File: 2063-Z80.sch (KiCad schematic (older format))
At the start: 80 parts, among them J1 Conn_01x05, J10 Conn_01x07, J11 Conn_02x03, J2 DM3D-SF(41), J3 Conn_02x20, J4 Conn_02x05, J5 Conn_02x05, J6 0548190519, J7 Conn_02x13, J8 Conn_01x05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

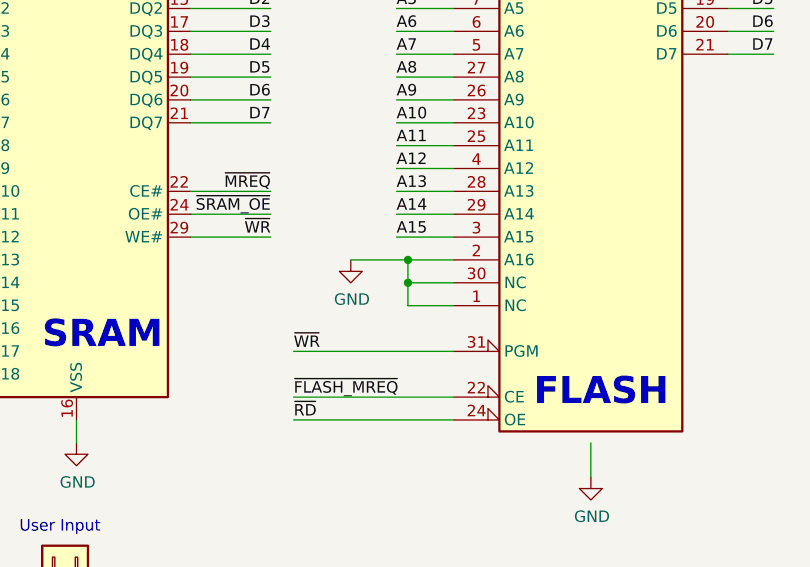
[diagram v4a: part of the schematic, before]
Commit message: Make pins U3.1 & U3.30 NC (easier for UV EPROM)
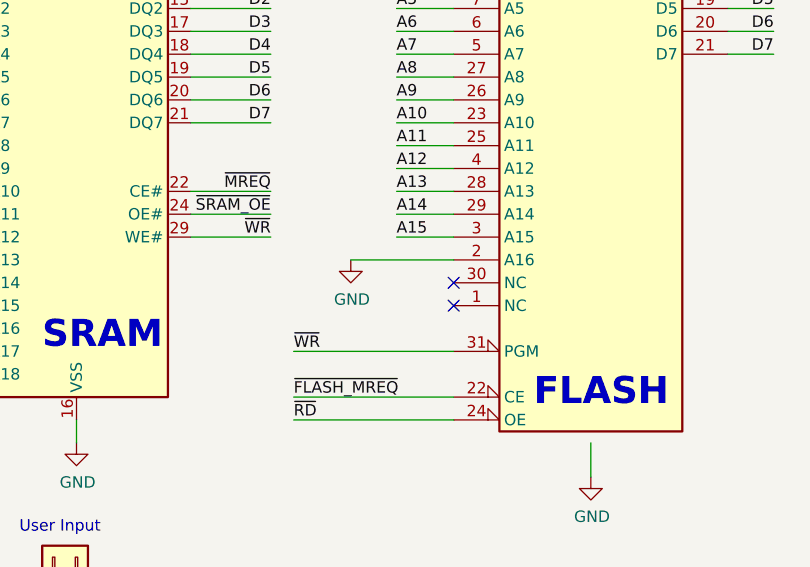
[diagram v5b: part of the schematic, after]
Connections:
- net GND: no longer U3.1 (NC), U3.30 (NC)
- no-connect marks 32 -> 34
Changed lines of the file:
@@
 Wire Wire Line
 	11050 9650 11050 9500
-Wire Wire Line
-	5400 4000 5200 4000
-Wire Wire Line
-	5200 4000 5200 4100
-Wire Wire Line
-	5400 4100 5200 4100
-Connection ~ 5200 4100
-Wire Wire Line
-	5200 4100 5200 4200
-Wire Wire Line
-	5400 4200 5200 4200
 $Comp
 L power:+5V #PWR0141
@@
 	1    0    0    -1
 $EndComp
-Wire Wire Line
-	6000 4800 6000 4950
 Text Label 4700 4600 0    50   ~ 0
 ~FLASH_MREQ
@@
 	1    0    0    -1
 $EndComp
-Wire Wire Line
-	4950 4000 5200 4000
-Connection ~ 5200 4000
 Wire Wire Line
 	8100 6100 8450 6100
@@
 $EndComp
 $Comp
-L Memory_Flash:SST39SF010 U3
-U 1 1 62897764
-P 6000 3600
-F 0 "U3" H 6450 5050 50  0000 C CNN
-F 1 "SST39SF010" H 6450 4950 50  0000 C CNN
-F 2 "Package_DIP:DIP-32_W15.24mm_Socket" H 6000 3900 50  0001 C CNN
-F 3 "https://ww1.microchip.com/downloads/en/DeviceDoc/20005022C.pdf" H 6000 3900 50  0001 C CNN
-F 4 "IC FLASH 1MBIT PARALLEL 32DIP" H 6000 3600 50  0001 C CNN "Description"
-F 5 "SST39SF010A-70-4C-PHE-ND‎" H 6000 3600 50  0001 C CNN "Digi-Key_PN"
-F 6 "SST39SF010A-70-4C-PHE" H 6000 3600 50  0001 C CNN "MPN"
-F 7 "Microchip Technology" H 6000 3600 50  0001 C CNN "Manufacturer"
-	1    6000 3600
-	1    0    0    -1
-$EndComp
-$Comp
 L Device:R_Network08 RN2
 U 1 1 61079B79
@@
 Text Label 13850 6550 2    50   ~ 0
 ~DTRB
+Wire Wire Line
+	4950 4000 5400 4000
+Wire Wire Line
+	6000 4800 6000 4950
+$Comp
+L Memory_Flash:SST39SF010 U3
+U 1 1 62897764
+P 6000 3600
+F 0 "U3" H 6450 5050 50  0000 C CNN
+F 1 "SST39SF010" H 6450 4950 50  0000 C CNN
+F 2 "Package_DIP:DIP-32_W15.24mm_Socket" H 6000 3900 50  0001 C CNN
+F 3 "https://ww1.microchip.com/downloads/en/DeviceDoc/20005022C.pdf" H 6000 3900 50  0001 C CNN
+F 4 "IC FLASH 1MBIT PARALLEL 32DIP" H 6000 3600 50  0001 C CNN "Description"
+F 5 "SST39SF010A-70-4C-PHE-ND‎" H 6000 3600 50  0001 C CNN "Digi-Key_PN"
+F 6 "SST39SF010A-70-4C-PHE" H 6000 3600 50  0001 C CNN "MPN"
+F 7 "Microchip Technology" H 6000 3600 50  0001 C CNN "Manufacturer"
+	1    6000 3600
+	1    0    0    -1
+$EndComp
+NoConn ~ 5400 4100
+NoConn ~ 5400 4200
 $EndSCHEMATC

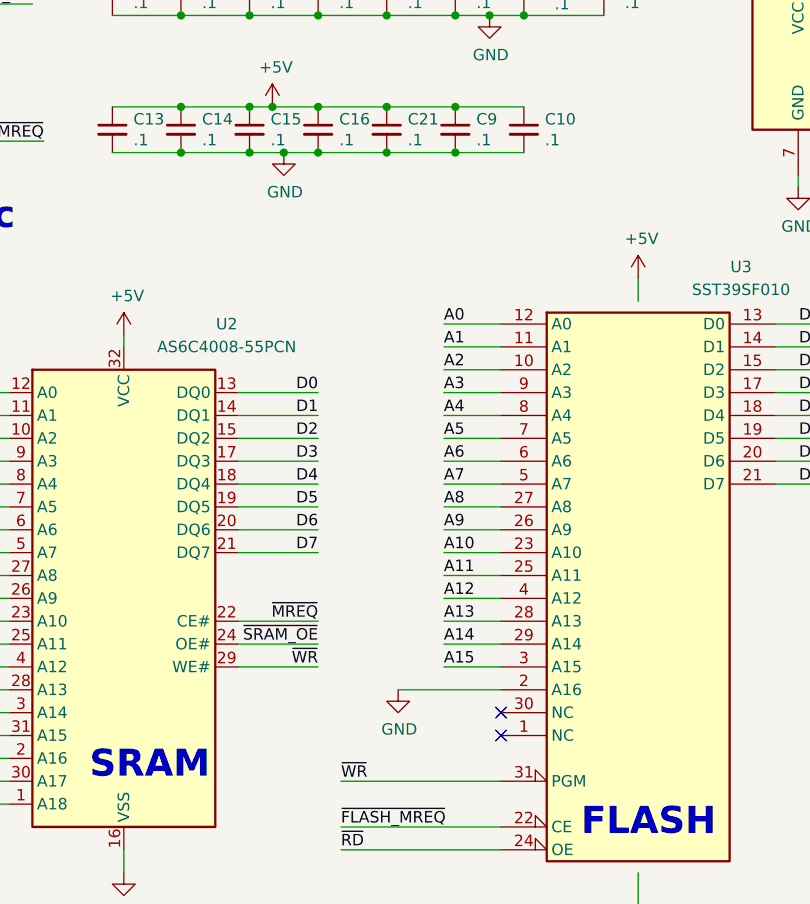
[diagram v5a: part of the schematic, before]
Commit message: Add pulldown & J12 to A16 for FLASH bank select
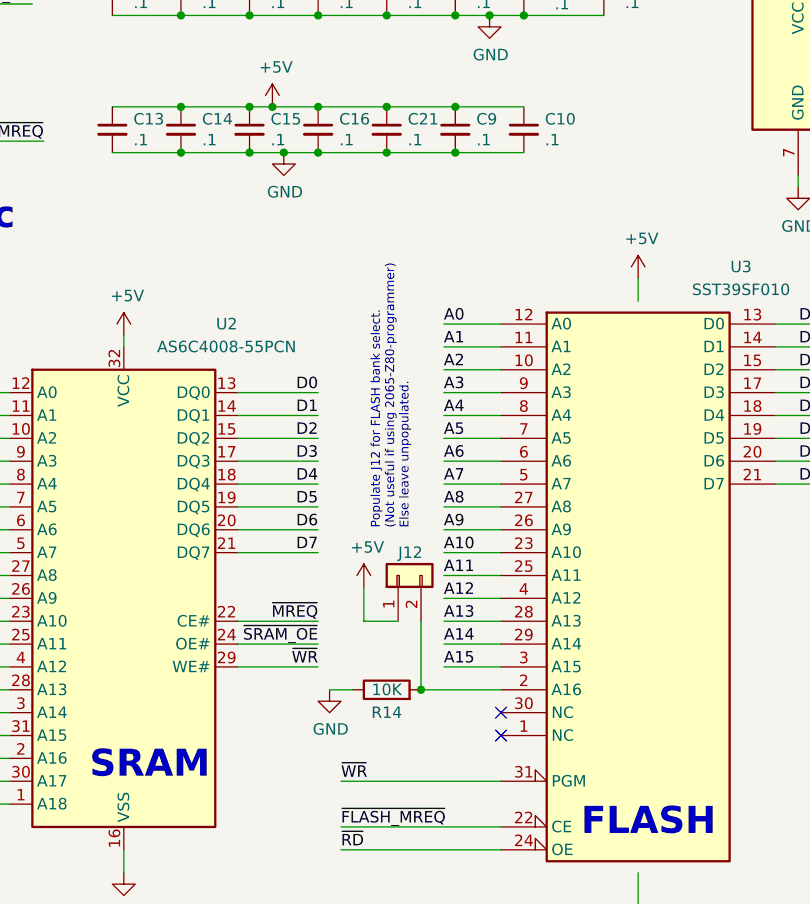
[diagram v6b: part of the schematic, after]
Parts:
- added J12: Conn_01x02, Connector_PinHeader_2.54mm:PinHeader_1x02_P2.54mm_Vertical, symbol Connector_Generic:Conn_01x02
- added R14: 10K, Resistor_THT:R_Axial_DIN0204_L3.6mm_D1.6mm_P5.08mm_Horizontal, symbol Device:R
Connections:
- net +5V: now also J12.1 (Pin_1)
- net GND: now also R14.1; no longer U3.2 (A16)
- new net: J12.2 (Pin_2), R14.2, U3.2 (A16)
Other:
- note added: "Populate J12 for FLASH bank select.\n(Not useful if using 2065-Z80-programmer)\nElse leave unpopulated."
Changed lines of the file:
@@
 L power:GND #PWR010
 U 1 1 62F49F76
-P 4950 4000
-F 0 "#PWR010" H 4950 3750 50  0001 C CNN
-F 1 "GND" H 4955 3827 50  0000 C CNN
-F 2 "" H 4950 4000 50  0001 C CNN
-F 3 "" H 4950 4000 50  0001 C CNN
-	1    4950 4000
+P 4650 4000
+F 0 "#PWR010" H 4650 3750 50  0001 C CNN
+F 1 "GND" H 4655 3827 50  0000 C CNN
+F 2 "" H 4650 4000 50  0001 C CNN
+F 3 "" H 4650 4000 50  0001 C CNN
+	1    4650 4000
 	1    0    0    -1
 $EndComp
@@
 ~DTRB
 Wire Wire Line
-	4950 4000 5400 4000
-Wire Wire Line
 	6000 4800 6000 4950
 $Comp
@@
 NoConn ~ 5400 4100
 NoConn ~ 5400 4200
+$Comp
+L Device:R R14
+U 1 1 61ED6941
+P 4900 4000
+F 0 "R14" V 4800 4000 50  0000 C CNN
+F 1 "10K" V 4900 4000 50  0000 C CNN
+F 2 "Resistor_THT:R_Axial_DIN0204_L3.6mm_D1.6mm_P5.08mm_Horizontal" V 4830 4000 50  0001 C CNN
+F 3 "https://www.seielect.com/catalog/sei-cf_cfm.pdf" H 4900 4000 50  0001 C CNN
+F 4 "RES 10K OHM 5% 1/8W AXIAL" H 4900 4000 50  0001 C CNN "Description"
+F 5 "CF18JT10K0CT-ND" H 4900 4000 50  0001 C CNN "Digi-Key_PN"
+F 6 "CF18JT10K0" H 4900 4000 50  0001 C CNN "MPN"
+F 7 "Stackpole Electronics Inc" H 4900 4000 50  0001 C CNN "Manufacturer"
+	1    4900 4000
+	0    -1   -1   0
+$EndComp
+Wire Wire Line
+	4650 4000 4750 4000
+$Comp
+L Connector_Generic:Conn_01x02 J12
+U 1 1 62007C5F
+P 4950 3500
+F 0 "J12" V 5050 3500 50  0000 R CNN
+F 1 "Conn_01x02" V 4823 3312 50  0001 R CNN
+F 2 "Connector_PinHeader_2.54mm:PinHeader_1x02_P2.54mm_Vertical" H 4950 3500 50  0001 C CNN
+F 3 "https://media.digikey.com/PDF/Data%20Sheets/Sullins%20PDFs/xRxCzzzSxxN-RC_ST_11635-B.pdf" H 4950 3500 50  0001 C CNN
+F 4 "CONN HEADER VERT 2POS 2.54MM" H 4950 3500 50  0001 C CNN "Description"
+F 5 "S1011EC-02-ND" H 4950 3500 50  0001 C CNN "Digi-Key_PN"
+F 6 "PRPC002SAAN-RC" H 4950 3500 50  0001 C CNN "MPN"
+F 7 "Sullins Connector Solutions" H 4950 3500 50  0001 C CNN "Manufacturer"
+	1    4950 3500
+	0    -1   -1   0
+$EndComp
+Wire Wire Line
+	5050 4000 5400 4000
+Connection ~ 5050 4000
+Wire Wire Line
+	4950 3700 4800 3700
+Wire Wire Line
+	4800 3700 4800 3550
+$Comp
+L power:+5V #PWR019
+U 1 1 62228824
+P 4800 3550
+F 0 "#PWR019" H 4800 3400 50  0001 C CNN
+F 1 "+5V" H 4815 3723 50  0000 C CNN
+F 2 "" H 4800 3550 50  0001 C CNN
+F 3 "" H 4800 3550 50  0001 C CNN
+	1    4800 3550
+	1    0    0    -1
+$EndComp
+Wire Wire Line
+	5050 3700 5050 4000
+Text Notes 5000 3300 1    39   ~ 0
+Populate J12 for FLASH bank select.\n(Not useful if using 2065-Z80-programmer)\nElse leave unpopulated.
 $EndSCHEMATC

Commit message: Terminate the clock traces.
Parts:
- added R15, R16: 120, Resistor_THT:R_Axial_DIN0204_L3.6mm_D1.6mm_P5.08mm_Horizontal, symbol Device:R
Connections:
- net BAUD_CLK: now also R16.2
- net CLK: now also R15.2
- net GND: now also R15.1, R16.1
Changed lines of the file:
@@
 CLK
 Wire Wire Line
-	9050 1200 9350 1200
+	9050 1200 9150 1200
 Text Label 9350 1200 2    50   ~ 0
 CLK
@@
 Connection ~ 12200 2200
 Wire Wire Line
-	12200 2200 12600 2200
-Wire Wire Line
 	11250 2900 12200 2900
 Wire Wire Line
@@
 Text Notes 5000 3300 1    39   ~ 0
 Populate J12 for FLASH bank select.\n(Not useful if using 2065-Z80-programmer)\nElse leave unpopulated.
+Wire Wire Line
+	9150 1500 9150 1200
+Connection ~ 9150 1200
+Wire Wire Line
+	9150 1200 9350 1200
+Wire Wire Line
+	9450 1500 9550 1500
+$Comp
+L power:GND #PWR020
+U 1 1 61C29EFA
+P 9550 1500
+F 0 "#PWR020" H 9550 1250 50  0001 C CNN
+F 1 "GND" H 9555 1327 50  0000 C CNN
+F 2 "" H 9550 1500 50  0001 C CNN
+F 3 "" H 9550 1500 50  0001 C CNN
+	1    9550 1500
+	1    0    0    -1
+$EndComp
+$Comp
+L Device:R R16
+U 1 1 61C3AA3E
+P 12850 2200
+F 0 "R16" V 12750 2200 50  0000 C CNN
+F 1 "120" V 12850 2200 50  0000 C CNN
+F 2 "Resistor_THT:R_Axial_DIN0204_L3.6mm_D1.6mm_P5.08mm_Horizontal" V 12780 2200 50  0001 C CNN
+F 3 "https://www.seielect.com/catalog/sei-cf_cfm.pdf" H 12850 2200 50  0001 C CNN
+F 4 "RES 120 OHM 5% 1/8W AXIAL" H 12850 2200 50  0001 C CNN "Description"
+F 5 "CF18JT120RCT-ND" H 12850 2200 50  0001 C CNN "Digi-Key_PN"
+F 6 "CF18JT120R" H 12850 2200 50  0001 C CNN "MPN"
+F 7 "Stackpole Electronics Inc" H 12850 2200 50  0001 C CNN "Manufacturer"
+	1    12850 2200
+	0    1    1    0
+$EndComp
+Wire Wire Line
+	13000 2200 13100 2200
+$Comp
+L power:GND #PWR021
+U 1 1 61C3AA46
+P 13100 2200
+F 0 "#PWR021" H 13100 1950 50  0001 C CNN
+F 1 "GND" H 13105 2027 50  0000 C CNN
+F 2 "" H 13100 2200 50  0001 C CNN
+F 3 "" H 13100 2200 50  0001 C CNN
+	1    13100 2200
+	1    0    0    -1
+$EndComp
+Wire Wire Line
+	12200 2200 12700 2200
+$Comp
+L Device:R R15
+U 1 1 61D53855
+P 9300 1500
+F 0 "R15" V 9200 1500 50  0000 C CNN
+F 1 "120" V 9300 1500 50  0000 C CNN
+F 2 "Resistor_THT:R_Axial_DIN0204_L3.6mm_D1.6mm_P5.08mm_Horizontal" V 9230 1500 50  0001 C CNN
+F 3 "https://www.seielect.com/catalog/sei-cf_cfm.pdf" H 9300 1500 50  0001 C CNN
+F 4 "RES 120 OHM 5% 1/8W AXIAL" H 9300 1500 50  0001 C CNN "Description"
+F 5 "CF18JT120RCT-ND" H 9300 1500 50  0001 C CNN "Digi-Key_PN"
+F 6 "CF18JT120R" H 9300 1500 50  0001 C CNN "MPN"
+F 7 "Stackpole Electronics Inc" H 9300 1500 50  0001 C CNN "Manufacturer"
+	1    9300 1500
+	0    1    1    0
+$EndComp
 $EndSCHEMATC
